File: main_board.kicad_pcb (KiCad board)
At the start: 2 copper layers, 1 part, among them U1 socket_leon_x3_dil64

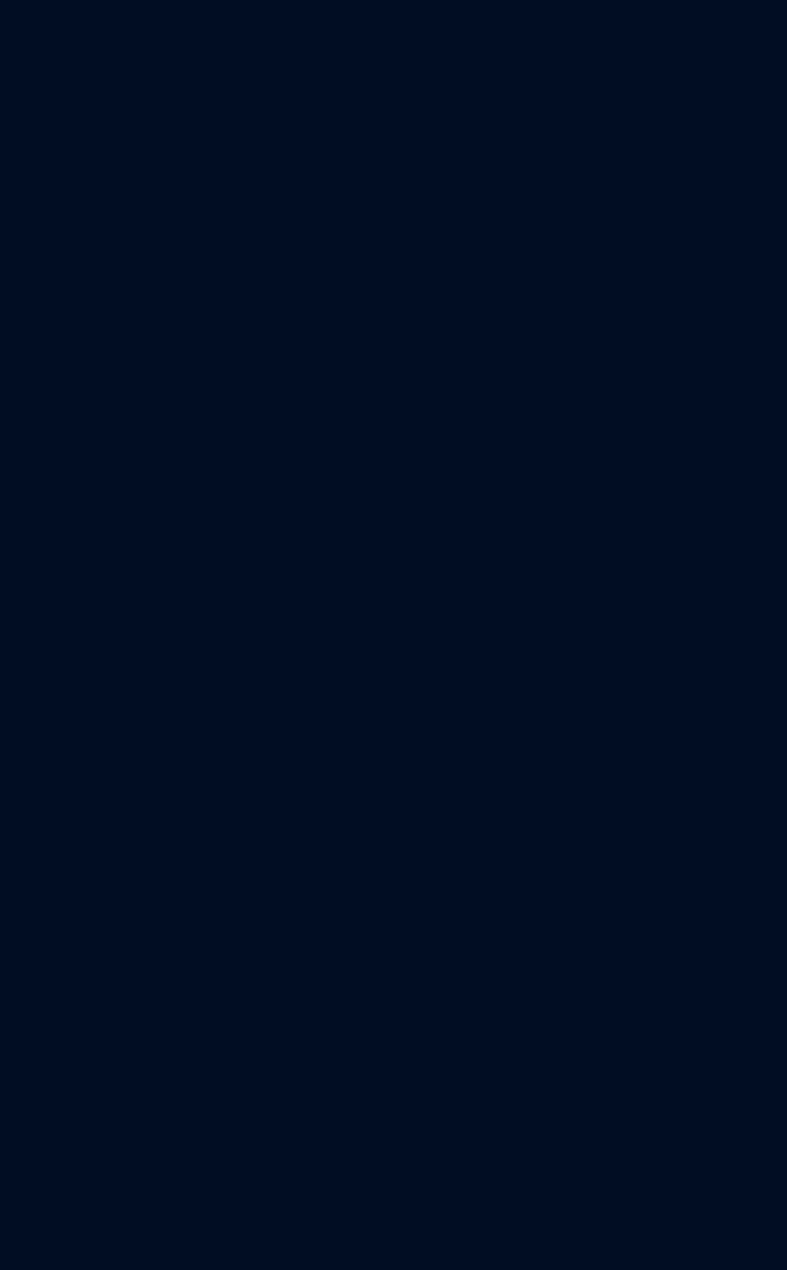
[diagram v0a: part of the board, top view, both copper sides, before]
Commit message: all: add pololu 24v12 footprint and symbol
Signed-off-by: Yannick Gicquel <ygicquel@gmail.com>
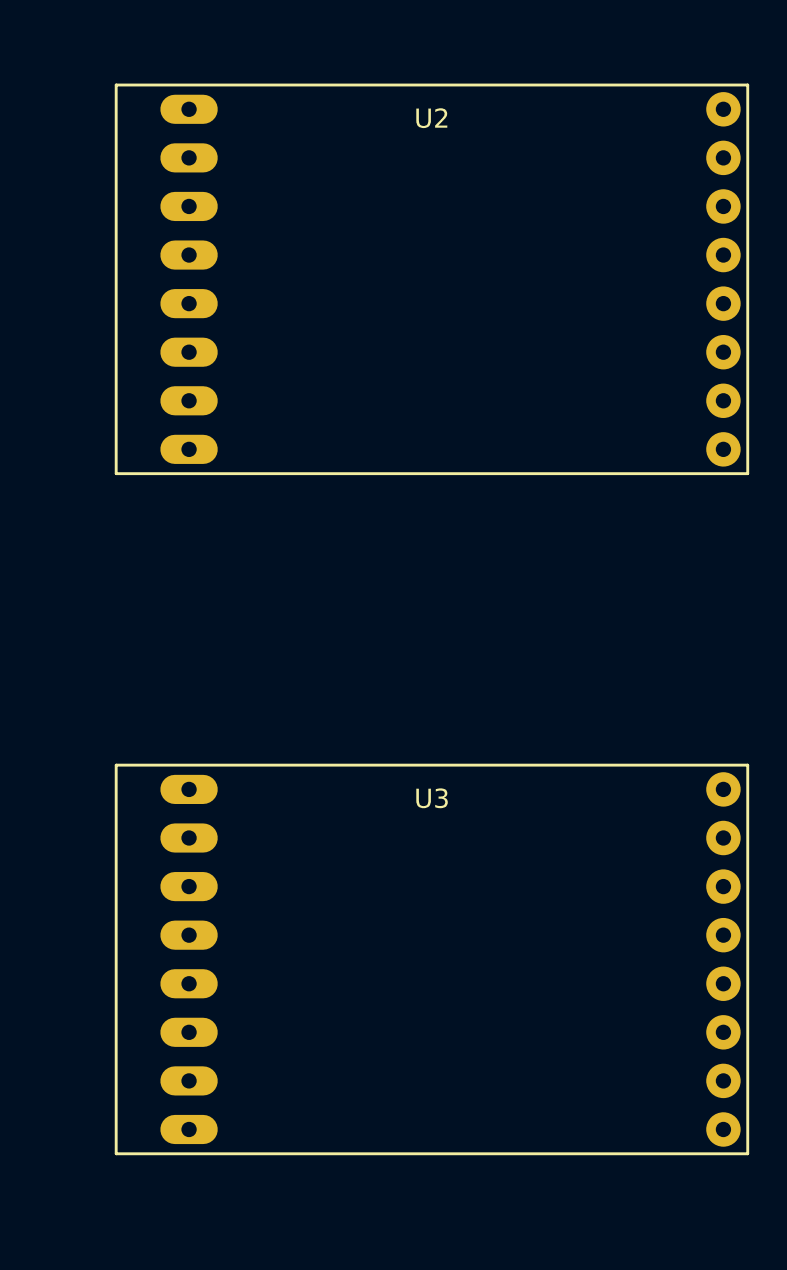
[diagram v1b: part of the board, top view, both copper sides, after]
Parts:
- added U2: socket_pololu_24v12, bot_parts:pololu_24v12_dip, F.Cu at (149.9, 67.3)
- added U3: socket_pololu_24v12, bot_parts:pololu_24v12_dip, F.Cu at (149.9, 102.9)
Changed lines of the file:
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@@
     (tracks 0)
     (zones 0)
-    (modules 1)
-    (nets 65)
+    (modules 3)
+    (nets 97)
   )
   (page A4)
@@
   (net 63 "Net-(U1-Pad63)")
   (net 64 "Net-(U1-Pad64)")
+  (net 65 "Net-(U2-Pad1)")
+  (net 66 "Net-(U2-Pad2)")
+  (net 67 "Net-(U2-Pad3)")
+  (net 68 "Net-(U2-Pad4)")
+  (net 69 "Net-(U2-Pad5)")
+  (net 70 "Net-(U2-Pad6)")
+  (net 71 "Net-(U2-Pad7)")
+  (net 72 "Net-(U2-Pad8)")
+  (net 73 "Net-(U2-Pad9)")
+  (net 74 "Net-(U2-Pad10)")
+  (net 75 "Net-(U2-Pad12)")
+  (net 76 "Net-(U2-Pad13)")
+  (net 77 "Net-(U2-Pad14)")
+  (net 78 "Net-(U2-Pad15)")
+  (net 79 "Net-(U2-Pad16)")
+  (net 80 "Net-(U3-Pad1)")
+  (net 81 "Net-(U3-Pad2)")
+  (net 82 "Net-(U3-Pad3)")
+  (net 83 "Net-(U3-Pad4)")
+  (net 84 "Net-(U3-Pad5)")
+  (net 85 "Net-(U3-Pad6)")
+  (net 86 "Net-(U3-Pad7)")
+  (net 87 "Net-(U3-Pad8)")
+  (net 88 "Net-(U3-Pad9)")
+  (net 89 "Net-(U3-Pad10)")
+  (net 90 "Net-(U3-Pad11)")
+  (net 91 "Net-(U3-Pad12)")
+  (net 92 "Net-(U3-Pad13)")
+  (net 93 "Net-(U3-Pad14)")
+  (net 94 "Net-(U3-Pad15)")
+  (net 95 "Net-(U3-Pad16)")
+  (net 96 "Net-(U2-Pad11)")
   (net_class Default "This is the default net class."
     (clearance 0.2)
@@
     (add_net "Net-(U1-Pad8)")
     (add_net "Net-(U1-Pad9)")
+    (add_net "Net-(U2-Pad1)")
+    (add_net "Net-(U2-Pad10)")
+    (add_net "Net-(U2-Pad11)")
+    (add_net "Net-(U2-Pad12)")
+    (add_net "Net-(U2-Pad13)")
+    (add_net "Net-(U2-Pad14)")
+    (add_net "Net-(U2-Pad15)")
+    (add_net "Net-(U2-Pad16)")
+    (add_net "Net-(U2-Pad2)")
+    (add_net "Net-(U2-Pad3)")
+    (add_net "Net-(U2-Pad4)")
+    (add_net "Net-(U2-Pad5)")
+    (add_net "Net-(U2-Pad6)")
+    (add_net "Net-(U2-Pad7)")
+    (add_net "Net-(U2-Pad8)")
+    (add_net "Net-(U2-Pad9)")
+    (add_net "Net-(U3-Pad1)")
+    (add_net "Net-(U3-Pad10)")
+    (add_net "Net-(U3-Pad11)")
+    (add_net "Net-(U3-Pad12)")
+    (add_net "Net-(U3-Pad13)")
+    (add_net "Net-(U3-Pad14)")
+    (add_net "Net-(U3-Pad15)")
+    (add_net "Net-(U3-Pad16)")
+    (add_net "Net-(U3-Pad2)")
+    (add_net "Net-(U3-Pad3)")
+    (add_net "Net-(U3-Pad4)")
+    (add_net "Net-(U3-Pad5)")
+    (add_net "Net-(U3-Pad6)")
+    (add_net "Net-(U3-Pad7)")
+    (add_net "Net-(U3-Pad8)")
+    (add_net "Net-(U3-Pad9)")
   )
   (module Housings_DIP:DIP-64_W22.86mm_LongPads (layer F.Cu)
@@
     )
   )
+  (module bot_parts:pololu_24v12_dip (layer F.Cu)
+    (at 149.86 67.31)
+    (fp_text reference U2 (at 0 -8.39) (layer F.SilkS)
+      (effects (font (size 1 1) (thickness 0.15)))
+    )
+    (fp_text value socket_pololu_24v12 (at 0 8.39) (layer F.Fab)
+      (effects (font (size 1 1) (thickness 0.15)))
+    )
+    (fp_line (start -16.51 -10.16) (end 16.51 -10.16) (layer F.SilkS) (width 0.15))
+    (fp_line (start 16.51 -10.16) (end 16.51 10.16) (layer F.SilkS) (width 0.15))
+    (fp_line (start 16.51 10.16) (end -16.51 10.16) (layer F.SilkS) (width 0.15))
+    (fp_line (start -16.51 10.16) (end -16.51 -10.16) (layer F.SilkS) (width 0.15))
+    (pad 1 thru_hole oval (at -12.7 -8.89) (size 3 1.524) (drill 0.8) (layers *.Cu *.Mask F.SilkS)
+      (net 65 "Net-(U2-Pad1)"))
+    (pad 2 thru_hole oval (at -12.7 -6.35) (size 3 1.524) (drill 0.8) (layers *.Cu *.Mask F.SilkS)
+      (net 66 "Net-(U2-Pad2)"))
+    (pad 3 thru_hole oval (at -12.7 -3.81) (size 3 1.524) (drill 0.8) (layers *.Cu *.Mask F.SilkS)
+      (net 67 "Net-(U2-Pad3)"))
+    (pad 4 thru_hole oval (at -12.7 -1.27) (size 3 1.524) (drill 0.8) (layers *.Cu *.Mask F.SilkS)
+      (net 68 "Net-(U2-Pad4)"))
+    (pad 5 thru_hole oval (at -12.7 1.27) (size 3 1.524) (drill 0.8) (layers *.Cu *.Mask F.SilkS)
+      (net 69 "Net-(U2-Pad5)"))
+    (pad 6 thru_hole oval (at -12.7 3.81) (size 3 1.524) (drill 0.8) (layers *.Cu *.Mask F.SilkS)
+      (net 70 "Net-(U2-Pad6)"))
+    (pad 7 thru_hole oval (at -12.7 6.35) (size 3 1.524) (drill 0.8) (layers *.Cu *.Mask F.SilkS)
+      (net 71 "Net-(U2-Pad7)"))
+    (pad 8 thru_hole oval (at -12.7 8.89) (size 3 1.524) (drill 0.8) (layers *.Cu *.Mask F.SilkS)
+      (net 72 "Net-(U2-Pad8)"))
+    (pad 9 thru_hole circle (at 15.24 8.89) (size 1.8 1.8) (drill 0.8) (layers *.Cu *.Mask F.SilkS)
+      (net 73 "Net-(U2-Pad9)"))
+    (pad 10 thru_hole circle (at 15.24 6.35) (size 1.8 1.8) (drill 0.8) (layers *.Cu *.Mask F.SilkS)
+      (net 74 "Net-(U2-Pad10)"))
+    (pad 11 thru_hole circle (at 15.24 3.81) (size 1.8 1.8) (drill 0.8) (layers *.Cu *.Mask F.SilkS)
+      (net 96 "Net-(U2-Pad11)"))
+    (pad 12 thru_hole circle (at 15.24 1.27) (size 1.8 1.8) (drill 0.8) (layers *.Cu *.Mask F.SilkS)
+      (net 75 "Net-(U2-Pad12)"))
+    (pad 13 thru_hole circle (at 15.24 -1.27) (size 1.8 1.8) (drill 0.8) (layers *.Cu *.Mask F.SilkS)
+      (net 76 "Net-(U2-Pad13)"))
+    (pad 14 thru_hole circle (at 15.24 -3.81) (size 1.8 1.8) (drill 0.8) (layers *.Cu *.Mask F.SilkS)
+      (net 77 "Net-(U2-Pad14)"))
+    (pad 15 thru_hole circle (at 15.24 -6.35) (size 1.8 1.8) (drill 0.8) (layers *.Cu *.Mask F.SilkS)
+      (net 78 "Net-(U2-Pad15)"))
+    (pad 16 thru_hole circle (at 15.24 -8.89) (size 1.8 1.8) (drill 0.8) (layers *.Cu *.Mask F.SilkS)
+      (net 79 "Net-(U2-Pad16)"))
+  )
+  (module bot_parts:pololu_24v12_dip (layer F.Cu)
+    (at 149.86 102.87)
+    (fp_text reference U3 (at 0 -8.39) (layer F.SilkS)
+      (effects (font (size 1 1) (thickness 0.15)))
+    )
+    (fp_text value socket_pololu_24v12 (at 0 8.39) (layer F.Fab)
+      (effects (font (size 1 1) (thickness 0.15)))
+    )
+    (fp_line (start -16.51 -10.16) (end 16.51 -10.16) (layer F.SilkS) (width 0.15))
+    (fp_line (start 16.51 -10.16) (end 16.51 10.16) (layer F.SilkS) (width 0.15))
+    (fp_line (start 16.51 10.16) (end -16.51 10.16) (layer F.SilkS) (width 0.15))
+    (fp_line (start -16.51 10.16) (end -16.51 -10.16) (layer F.SilkS) (width 0.15))
+    (pad 1 thru_hole oval (at -12.7 -8.89) (size 3 1.524) (drill 0.8) (layers *.Cu *.Mask F.SilkS)
+      (net 80 "Net-(U3-Pad1)"))
+    (pad 2 thru_hole oval (at -12.7 -6.35) (size 3 1.524) (drill 0.8) (layers *.Cu *.Mask F.SilkS)
+      (net 81 "Net-(U3-Pad2)"))
+    (pad 3 thru_hole oval (at -12.7 -3.81) (size 3 1.524) (drill 0.8) (layers *.Cu *.Mask F.SilkS)
+      (net 82 "Net-(U3-Pad3)"))
+    (pad 4 thru_hole oval (at -12.7 -1.27) (size 3 1.524) (drill 0.8) (layers *.Cu *.Mask F.SilkS)
+      (net 83 "Net-(U3-Pad4)"))
+    (pad 5 thru_hole oval (at -12.7 1.27) (size 3 1.524) (drill 0.8) (layers *.Cu *.Mask F.SilkS)
+      (net 84 "Net-(U3-Pad5)"))
+    (pad 6 thru_hole oval (at -12.7 3.81) (size 3 1.524) (drill 0.8) (layers *.Cu *.Mask F.SilkS)
+      (net 85 "Net-(U3-Pad6)"))
+    (pad 7 thru_hole oval (at -12.7 6.35) (size 3 1.524) (drill 0.8) (layers *.Cu *.Mask F.SilkS)
+      (net 86 "Net-(U3-Pad7)"))
+    (pad 8 thru_hole oval (at -12.7 8.89) (size 3 1.524) (drill 0.8) (layers *.Cu *.Mask F.SilkS)
+      (net 87 "Net-(U3-Pad8)"))
+    (pad 9 thru_hole circle (at 15.24 8.89) (size 1.8 1.8) (drill 0.8) (layers *.Cu *.Mask F.SilkS)
+      (net 88 "Net-(U3-Pad9)"))
+    (pad 10 thru_hole circle (at 15.24 6.35) (size 1.8 1.8) (drill 0.8) (layers *.Cu *.Mask F.SilkS)
+      (net 89 "Net-(U3-Pad10)"))
+    (pad 11 thru_hole circle (at 15.24 3.81) (size 1.8 1.8) (drill 0.8) (layers *.Cu *.Mask F.SilkS)
+      (net 90 "Net-(U3-Pad11)"))
+    (pad 12 thru_hole circle (at 15.24 1.27) (size 1.8 1.8) (drill 0.8) (layers *.Cu *.Mask F.SilkS)
+      (net 91 "Net-(U3-Pad12)"))
+    (pad 13 thru_hole circle (at 15.24 -1.27) (size 1.8 1.8) (drill 0.8) (layers *.Cu *.Mask F.SilkS)
+      (net 92 "Net-(U3-Pad13)"))
+    (pad 14 thru_hole circle (at 15.24 -3.81) (size 1.8 1.8) (drill 0.8) (layers *.Cu *.Mask F.SilkS)
+      (net 93 "Net-(U3-Pad14)"))
+    (pad 15 thru_hole circle (at 15.24 -6.35) (size 1.8 1.8) (drill 0.8) (layers *.Cu *.Mask F.SilkS)
+      (net 94 "Net-(U3-Pad15)"))
+    (pad 16 thru_hole circle (at 15.24 -8.89) (size 1.8 1.8) (drill 0.8) (layers *.Cu *.Mask F.SilkS)
+      (net 95 "Net-(U3-Pad16)"))
+  )
 )

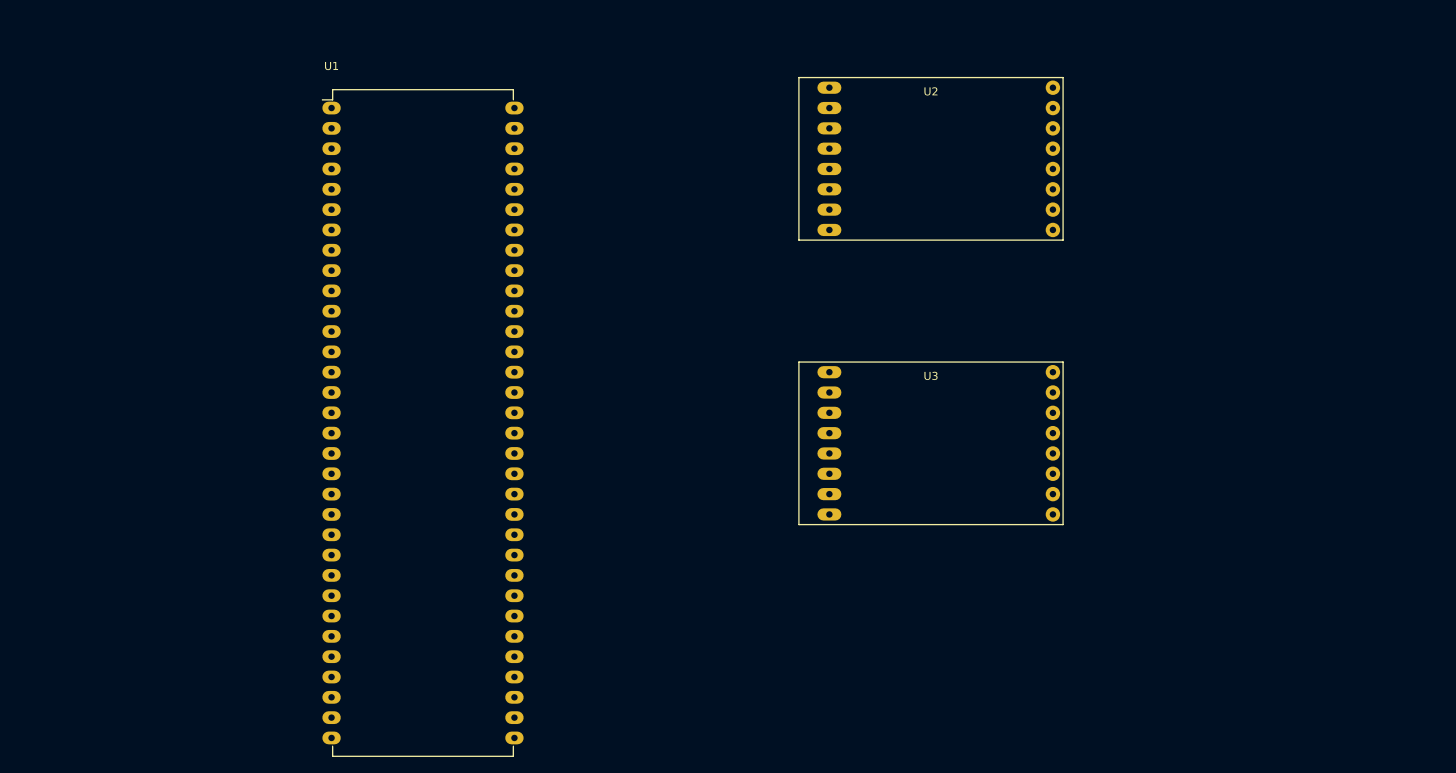
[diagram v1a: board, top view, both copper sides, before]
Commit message: pcb: add dimensions
same as geonobot "xmega_board" pcb.

Signed-off-by: Yannick Gicquel <ygicquel@gmail.com>
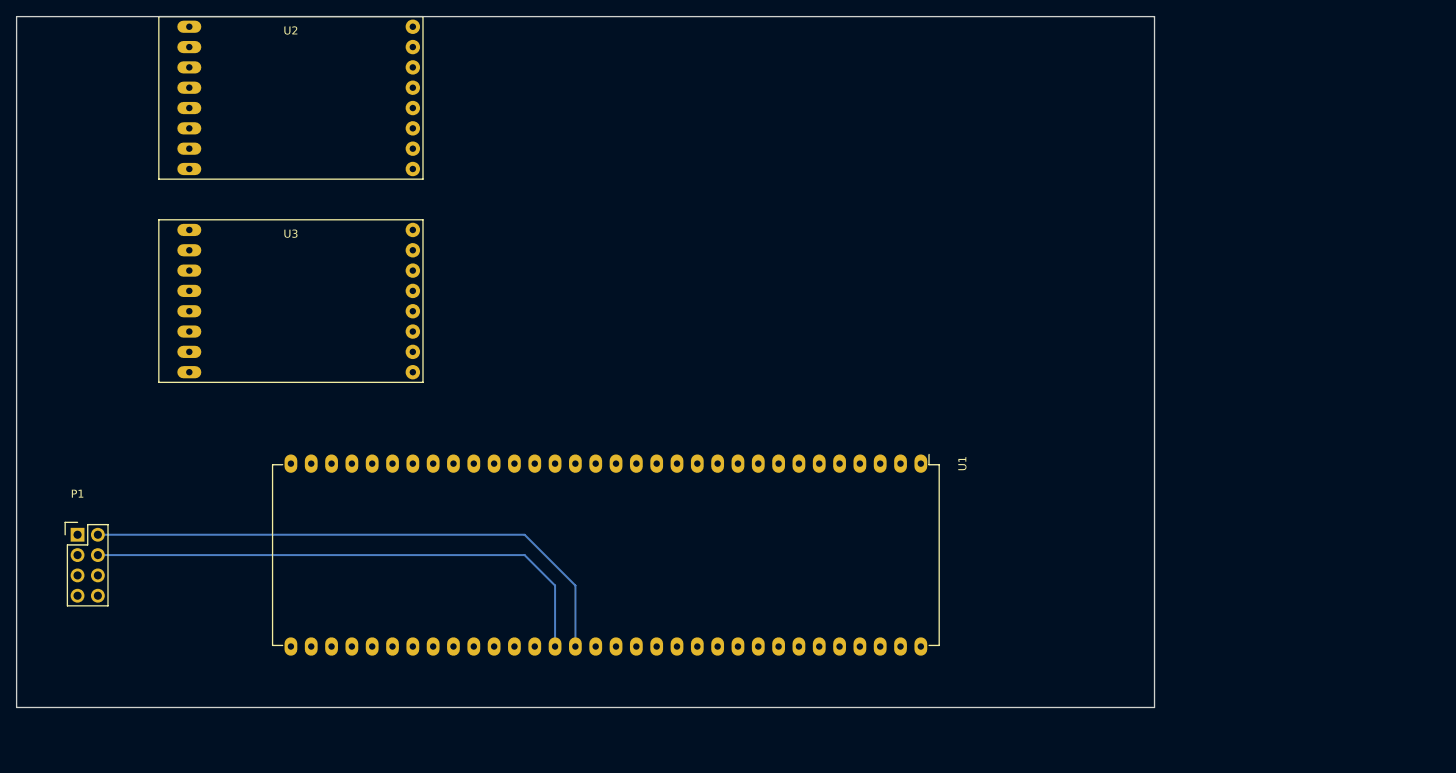
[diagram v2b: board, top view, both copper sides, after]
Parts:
- added P1: CONN_02X04, Pin_Headers:Pin_Header_Straight_2x04, F.Cu at (43.2, 114.3)
- moved U1 86.0 mm to (148.6, 105.4), turned to 270 degrees
- moved U3 82.0 mm to (69.8, 85.1)
- moved U2 80.4 mm to (69.8, 59.7)
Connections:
- U1 pad 30: Net-(U1-Pad30) -> DIR_L
- U1 pad 31: Net-(U1-Pad31) -> DIR_R
- U1 pad 36: Net-(U1-Pad36) -> PWM_L
- U1 pad 37: Net-(U1-Pad37) -> PWM_R
- U1 pad 39: Net-(U1-Pad39) -> ENC_A_L
- U1 pad 40: Net-(U1-Pad40) -> ENC_B_L
- U1 pad 46: Net-(U1-Pad46) -> ENC_A_R
- U1 pad 47: Net-(U1-Pad47) -> ENC_B_R
- U2 pad 1: Net-(U2-Pad1) -> +24V
- U2 pad 10: Net-(U2-Pad10) -> DIR_L
- U2 pad 11: Net-(U2-Pad11) -> PWM_L
- U2 pad 15: Net-(U2-Pad15) -> +24V
- U2 pad 16: Net-(U2-Pad16) -> +24V
- U2 pad 2: Net-(U2-Pad2) -> +24V
- U2 pad 3: Net-(U2-Pad3) -> OUTA_L
- U2 pad 4: Net-(U2-Pad4) -> OUTA_L
- U2 pad 5: Net-(U2-Pad5) -> OUTB_L
- U2 pad 6: Net-(U2-Pad6) -> OUTB_L
- U2 pad 7: Net-(U2-Pad7) -> GND
- U2 pad 8: Net-(U2-Pad8) -> GND
- U2 pad 9: Net-(U2-Pad9) -> GND
- U3 pad 1: Net-(U3-Pad1) -> +24V
- U3 pad 10: Net-(U3-Pad10) -> DIR_R
- U3 pad 11: Net-(U3-Pad11) -> PWM_R
- U3 pad 15: Net-(U3-Pad15) -> +24V
- U3 pad 16: Net-(U3-Pad16) -> +24V
- U3 pad 2: Net-(U3-Pad2) -> +24V
- U3 pad 3: Net-(U3-Pad3) -> OUTA_R
- U3 pad 4: Net-(U3-Pad4) -> OUTA_R
- U3 pad 5: Net-(U3-Pad5) -> OUTB_R
- U3 pad 6: Net-(U3-Pad6) -> OUTB_R
- U3 pad 7: Net-(U3-Pad7) -> GND
- U3 pad 8: Net-(U3-Pad8) -> GND
- U3 pad 9: Net-(U3-Pad9) -> GND
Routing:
- net ENC_B_R: track 0.00 -> 69.9 mm
- net ENC_A_R: track 0.00 -> 66.3 mm
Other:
- board outline added: 142.2 x 86.4 mm
